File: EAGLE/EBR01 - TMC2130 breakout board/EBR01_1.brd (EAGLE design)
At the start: 24.9 x 20.3 mm, 24 parts, among them J1 CPL-CON-HEADER-0.1IN-8P-M, J2 CPL-CON-HEADER-0.1IN-8P-M, J3 CPL-CON-HEADER-0.1IN-2X3P-M, Q1 CPL-REG-LIN-5V-0.1A, U1 TMC2130-LA

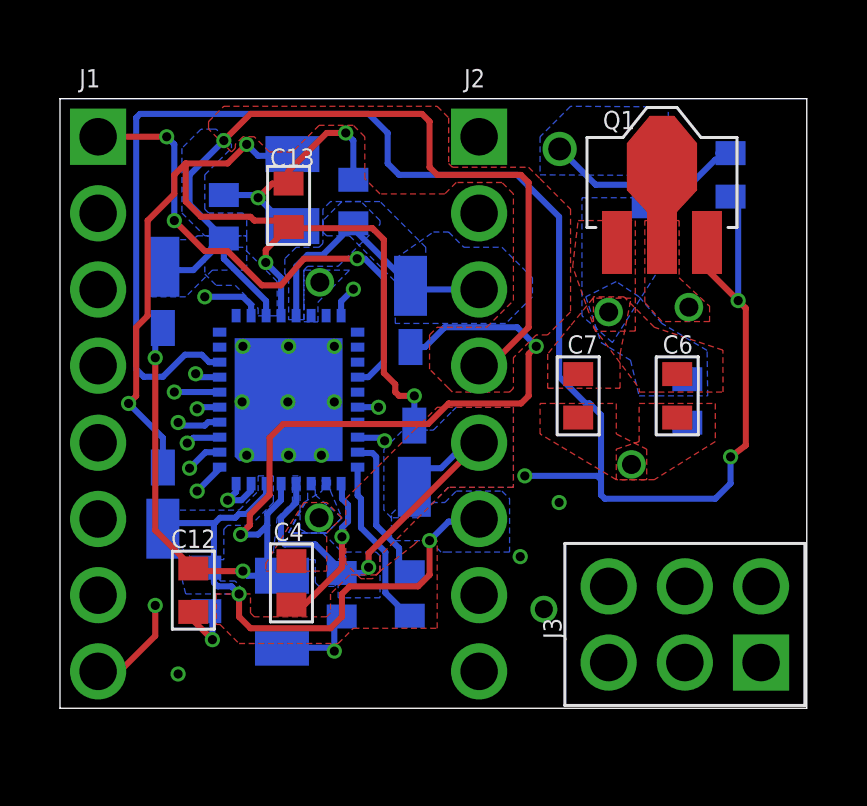
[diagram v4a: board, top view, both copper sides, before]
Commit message: Attempted to remove air wires.  Flipped R2 to eliminate vias on sense line.  Re-routed wires on ground plane and power plane.
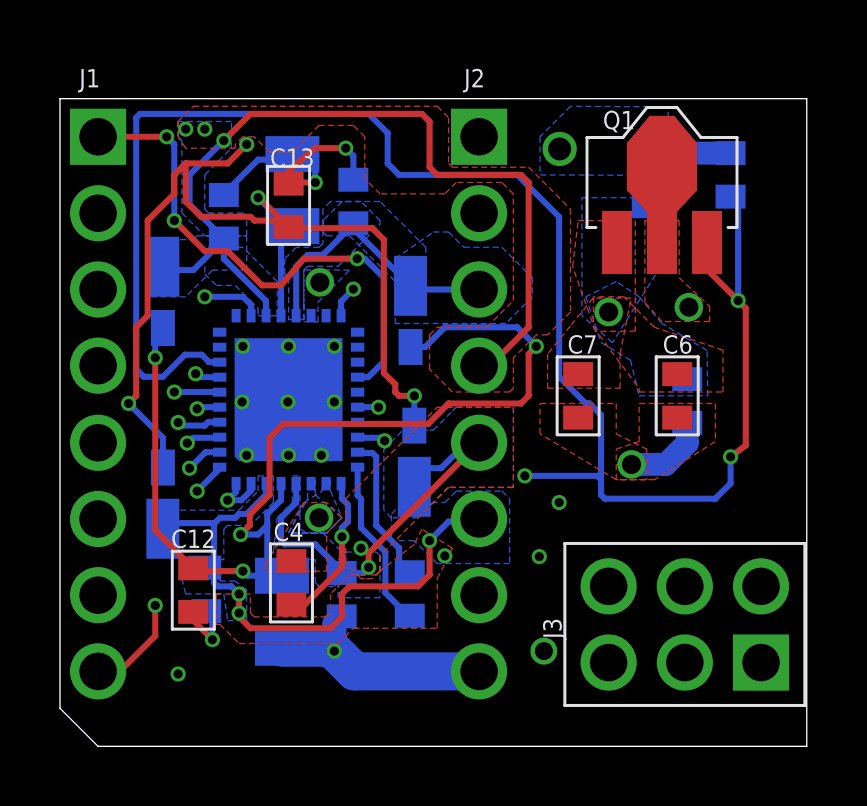
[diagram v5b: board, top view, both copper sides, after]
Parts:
- turned R2 to 270 degrees
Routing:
- net SPI_SDO: track 24.6 -> 50.3 mm
- net SPI_SCK: track 21.0 -> 33.4 mm
- net CLK: track 26.1 -> 32.7 mm
- net GND: track 26.5 -> 33.0 mm
- net SPI_!CS!: track 19.8 -> 24.0 mm
- net DIR: track 16.7 -> 13.3 mm
- net SPI_SDI: track 30.0 -> 31.2 mm
- net N$4: track 34.7 -> 35.6 mm
- net 2A: vias 1 -> 3
- net 1B: vias 2 -> 4
- net 1A: vias 1 -> 2
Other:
- board size 24.9 x 20.3 mm -> 24.9 x 21.6 mm

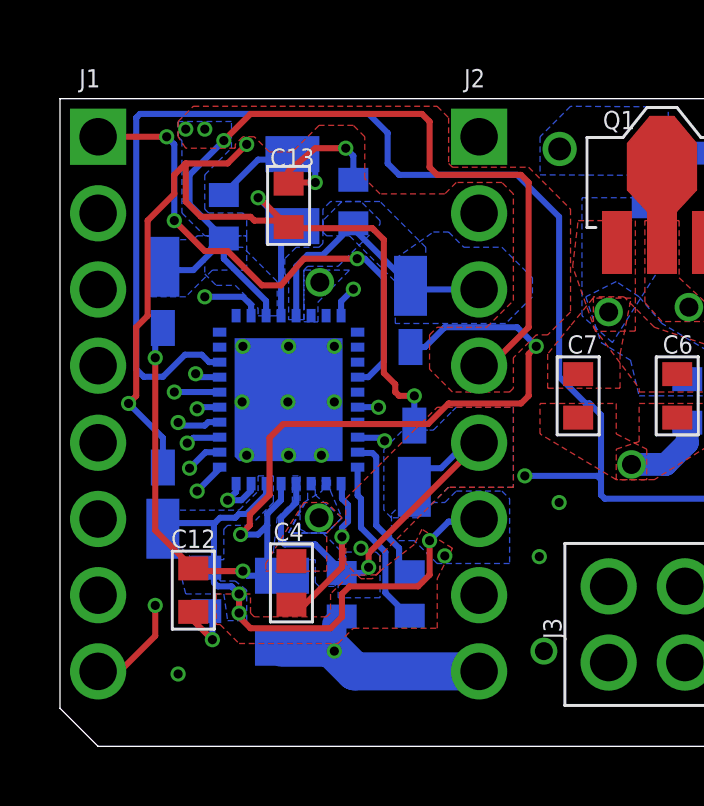
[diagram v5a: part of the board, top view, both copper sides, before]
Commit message: Corrected all (118) DRC errors for EBR01 board. Thickened traces for R2 GND connection, added extra vias to improve grounding, rerouted N$3 trace running directly under GND pad so more vias could be added for improved thermal protection. General tuneups of the traces were done. Corrected some of the nomenclature on the schematic to provide more detailed information.
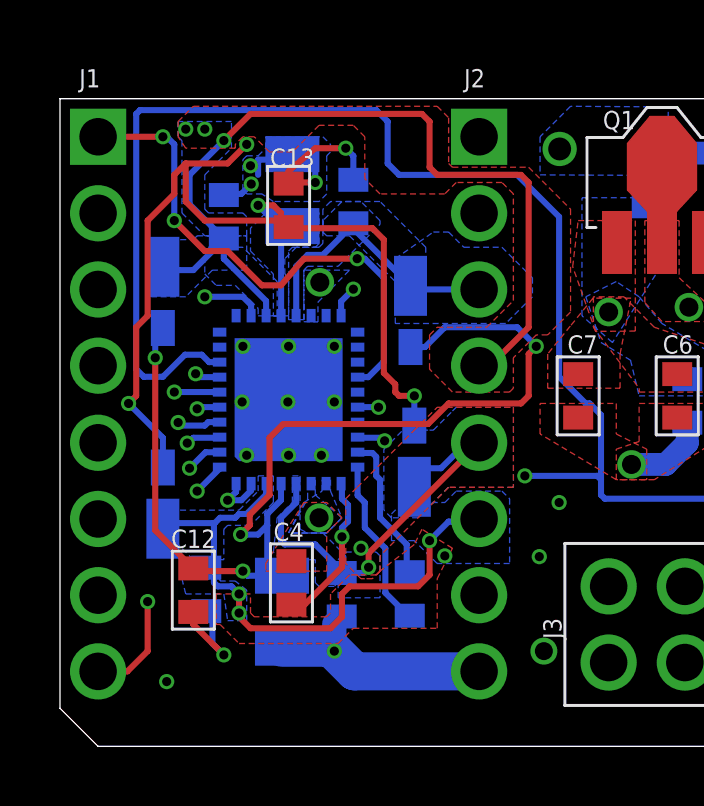
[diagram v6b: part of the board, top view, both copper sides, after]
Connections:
- net N$4 renamed BRB
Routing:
- net GND: track 33.0 -> 34.2 mm, vias 20 -> 22
- net CLK: track 32.7 -> 33.2 mm
- added copper zone on layer 16, net BRB

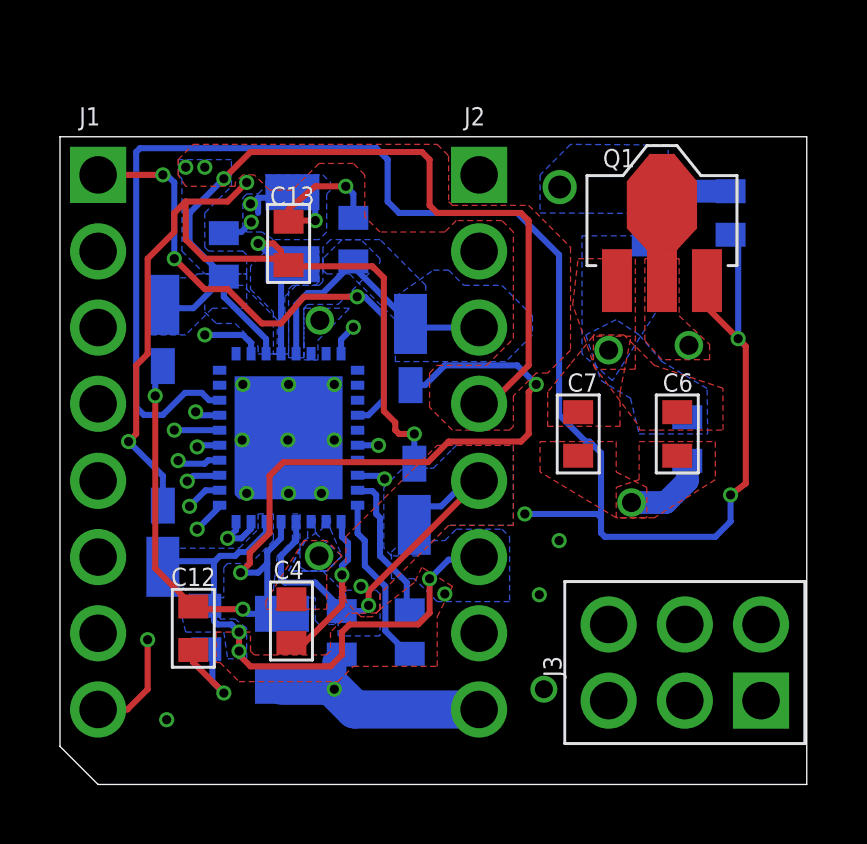
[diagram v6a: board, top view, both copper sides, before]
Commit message: Added vias to R1 GND connection, made all traces to GND wider. Moved board up so that Y=0 lines up with the bottom of the board and fixed Y dimension to reflect true height. Overall cleanup of vias and location.
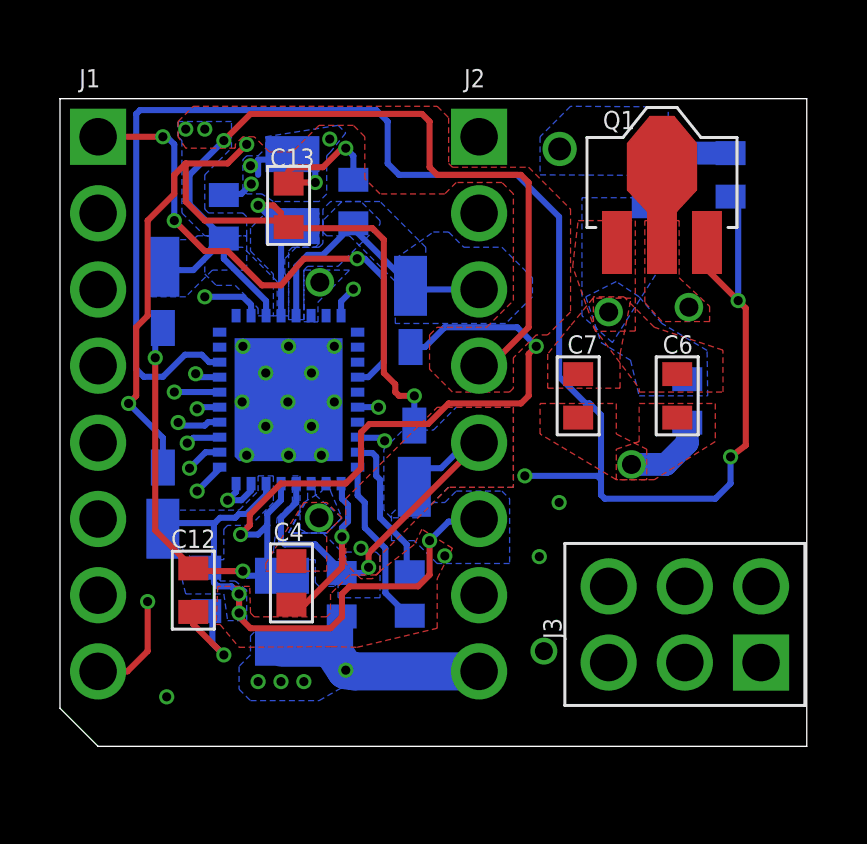
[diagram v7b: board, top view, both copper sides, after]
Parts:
- moved C8 1.27 mm to (9.78, 18.2)
- moved R2 1.27 mm to (7.75, 18.5)
- moved D1 1.27 mm to (11.7, 14.4)
- moved D2 1.27 mm to (3.43, 15.0)
- moved D4 1.27 mm to (3.43, 8.26)
- moved C11 1.27 mm to (4.88, 5.23)
- moved C12 1.27 mm to (4.44, 5.21)
- moved C5 1.27 mm to (11.7, 5.08)
- moved J3 1.27 mm to (20.8, 4.06)
- moved R1 1.27 mm to (7.40, 4.49)
- moved C1 1.27 mm to (20.9, 11.5)
- moved C10 1.27 mm to (9.39, 5.05)
- moved C13 1.27 mm to (7.62, 18.0)
- moved C2 1.27 mm to (19.6, 18.7)
- moved C3 1.27 mm to (22.4, 19.1)
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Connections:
- net N$3 renamed BRA
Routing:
- net SPI_!CS!: track 24.0 -> 25.9 mm
- net CLK: track 33.2 -> 34.3 mm
- net SPI_SDI: track 31.4 -> 32.5 mm
- net GND: track 34.2 -> 35.2 mm, vias 22 -> 30
- net SPI_SCK: track 33.4 -> 34.4 mm

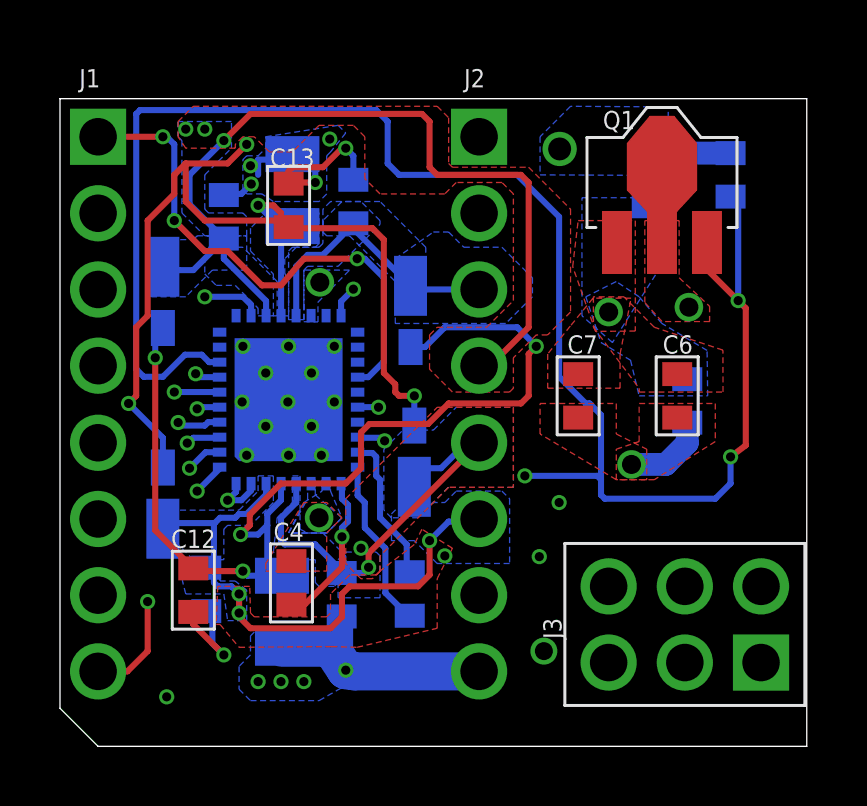
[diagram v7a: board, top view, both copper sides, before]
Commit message: Tweaked routing and placement on board.  This is the version that will be submitted to the board house.  Exported GERBERs and checked them in.
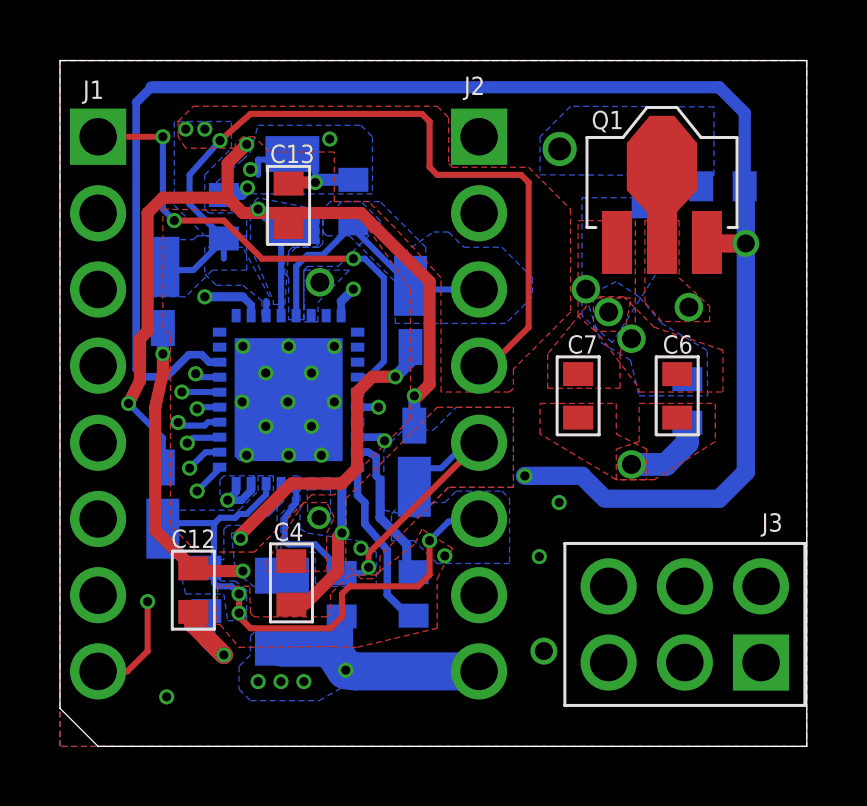
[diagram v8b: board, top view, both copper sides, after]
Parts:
- moved C3 0.46 mm to (22.1, 18.7), turned to 180 degrees
- moved C5 0.13 mm to (11.8, 5.08)
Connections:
- net N$1 renamed CPI
- net N$5 renamed CPO
- net N$8 renamed VCP
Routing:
- net BRA: track 35.3 -> 22.7 mm
- net GND: track 35.2 -> 31.7 mm, vias 30 -> 29
- net VCC: track 64.0 -> 60.6 mm, vias 4 -> 3
- net BRB: track 35.7 -> 32.5 mm
- net 2A: track 29.2 -> 27.3 mm
- net !ENABLE!: track 17.6 -> 16.8 mm
- added copper zone on layer 16, net BRA
- added copper zone on layer 15, net GND
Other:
- board size 24.9 x 21.6 mm -> 24.9 x 22.9 mm
